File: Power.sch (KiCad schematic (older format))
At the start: 10 parts, among them U2 MCP1700T-3302E/TT_

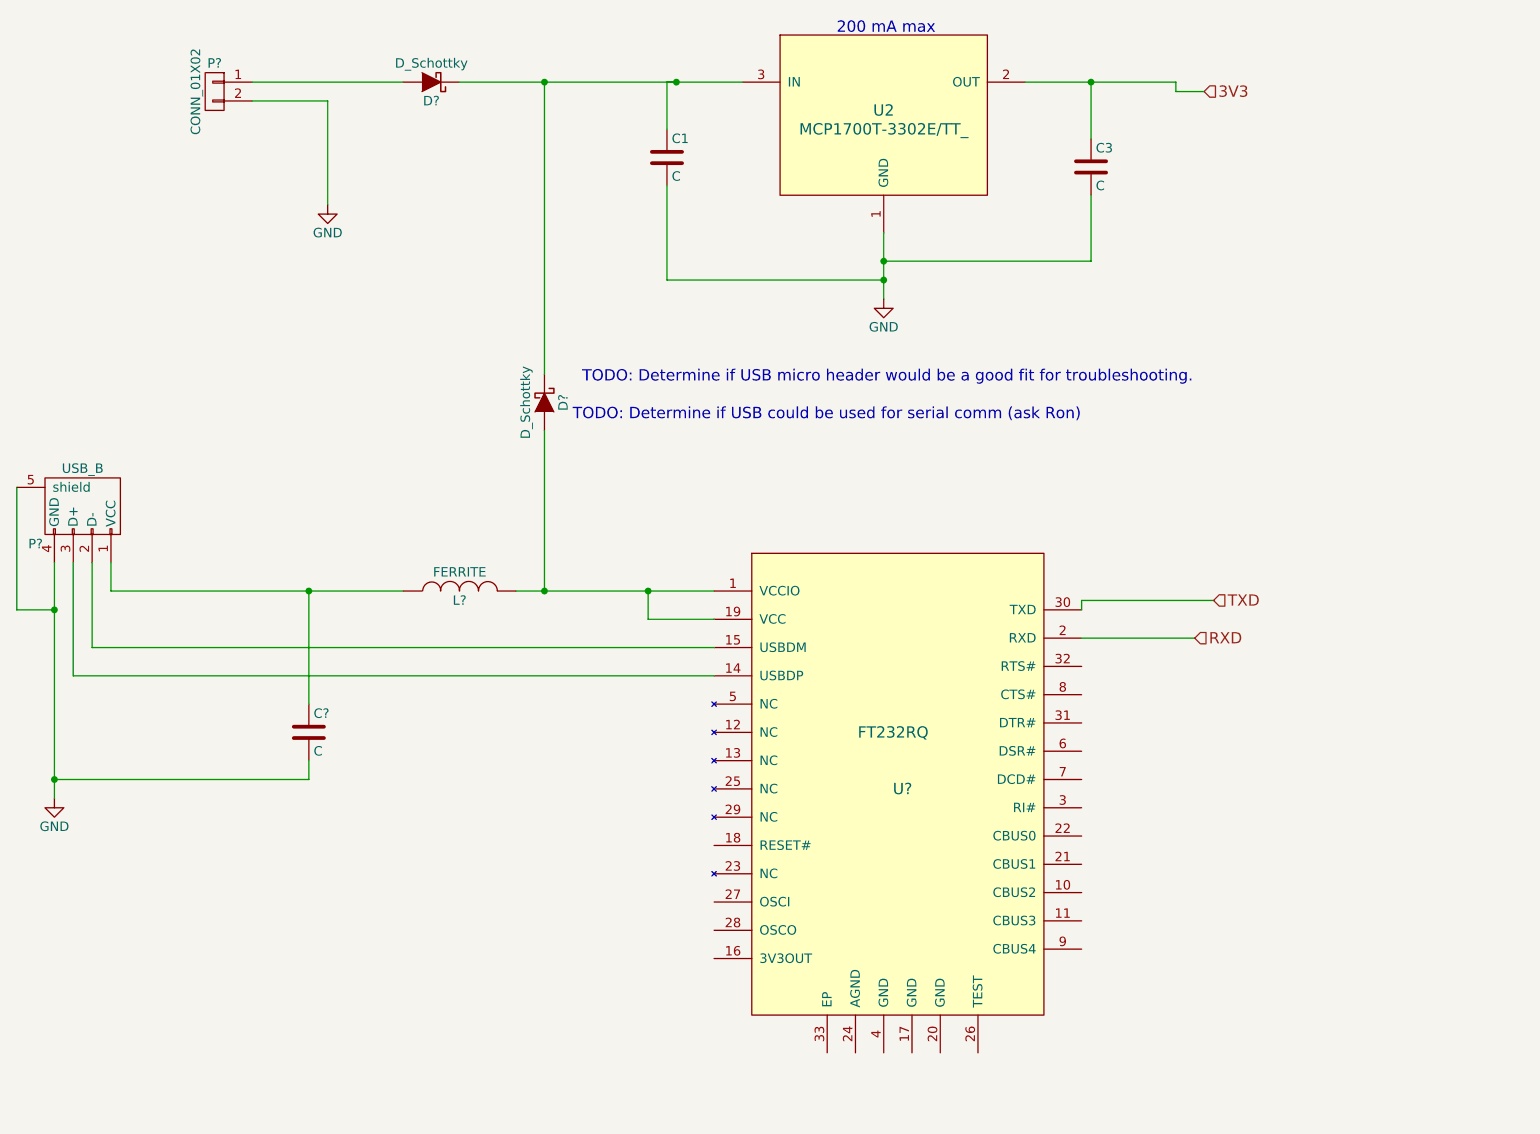
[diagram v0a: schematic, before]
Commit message: Added more decoupling caps, indicator LEDs and hooked reset into the FTDI chip
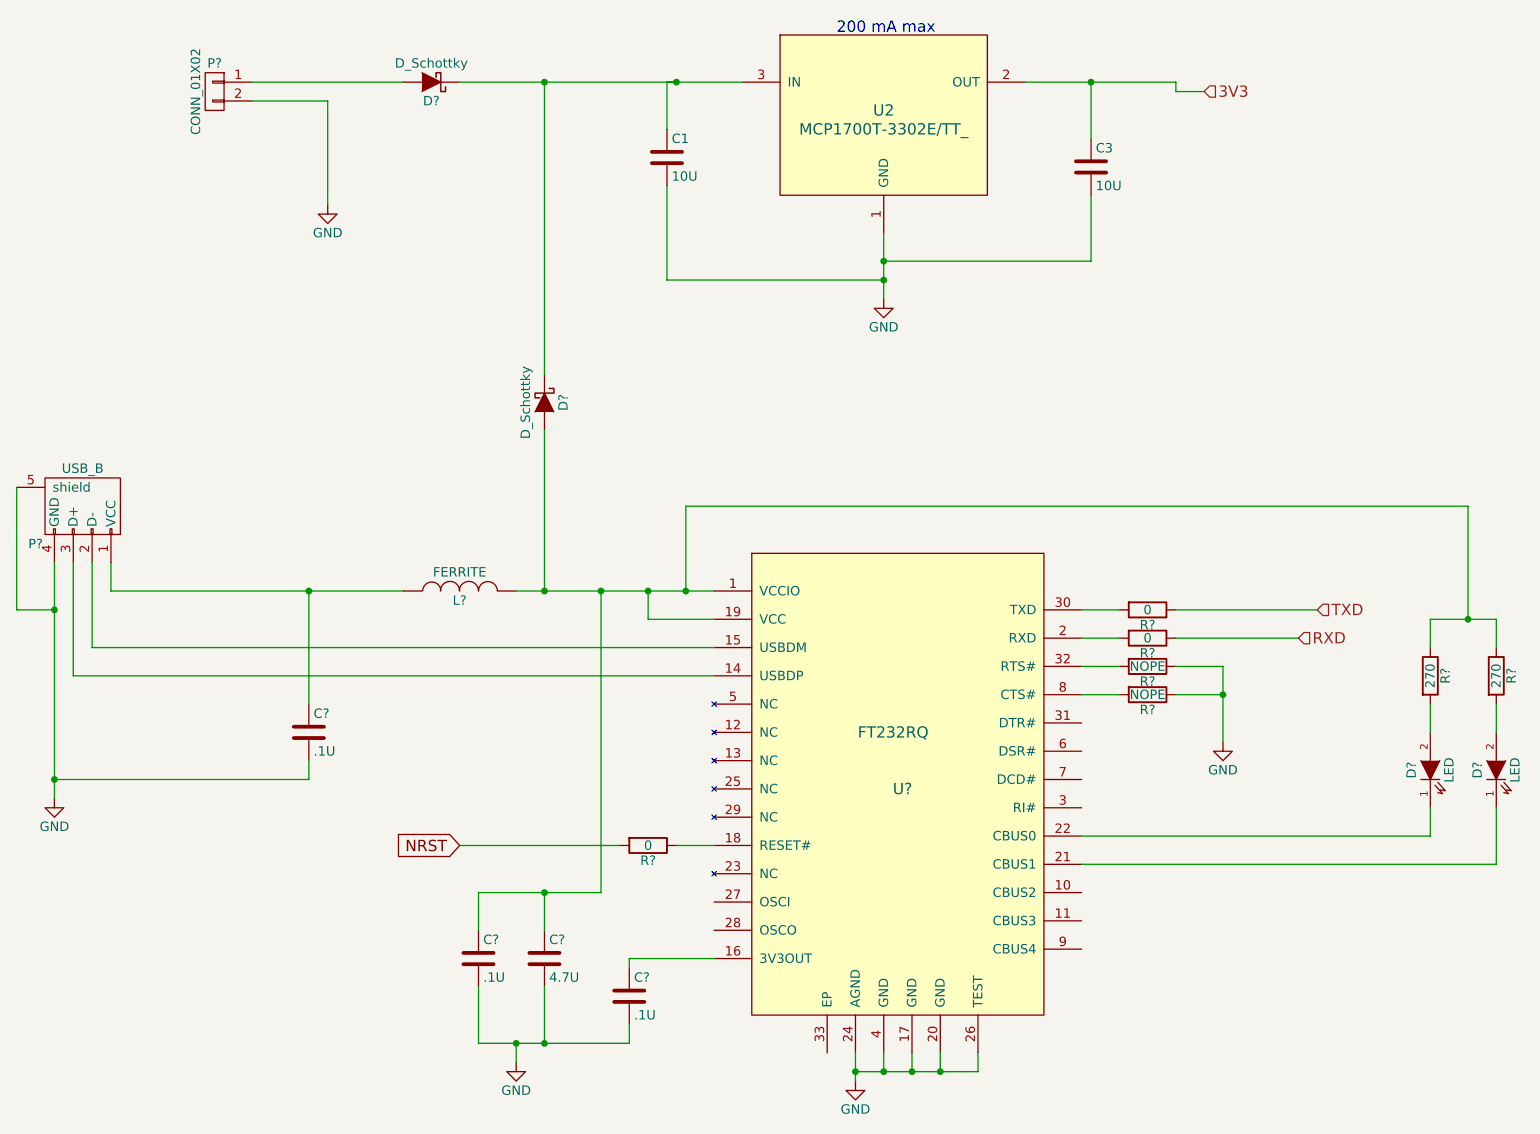
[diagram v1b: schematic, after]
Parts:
- added C?: 4.7U, symbol C
- added C? (x2): .1U, symbol C
- added D? (x2): LED, symbol LED
- added R? (x3): 0, symbol R
- added R? (x2): 270, symbol R
- added R? (x2): NOPE, symbol R
- C1, C3: value C -> 10U
- C?: value C -> .1U
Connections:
- net GND: now also U?.17 (GND), U?.20 (GND), U?.24 (AGND), U?.26 (TEST), U?.4 (GND), C?.2, C?.2, C?.2, R?.1, R?.1
- net RXD: now also R?.1; no longer U?.2 (RXD)
- net TXD: now also R?.1; no longer U?.30 (TXD)
- net at D?.2 (A), L?.2, U?.1 (VCCIO)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: now also C?.1, C?.1, R?.1, R?.1
- net at U?.16 (3V3OUT): now also C?.1
- net at U?.18 (RESET#): now also R?.1
- net at U?.21 (CBUS1): now also D?.1 (K)
- net at U?.22 (CBUS0): now also D?.1 (K)
- net at U?.32 (RTS#): now also R?.2
- net at U?.8 (CTS#): now also R?.2
- new net: R?.2, U?.2 (RXD)
- new net: R?.2, U?.30 (TXD)
- new net: D?.2 (A), R?.2 (x2)
- new net NRST: R?.2
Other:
- note removed: "TODO: Determine if USB could be used for serial comm (ask Ron)"
- note removed: "TODO: Determine if USB micro header would be a good fit for troubleshooting."

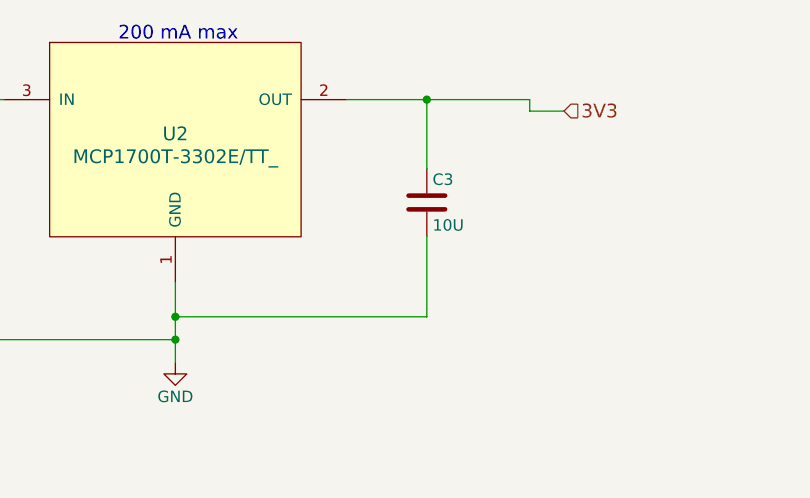
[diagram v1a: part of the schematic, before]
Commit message: Added headers and created a new sheet for communication headers
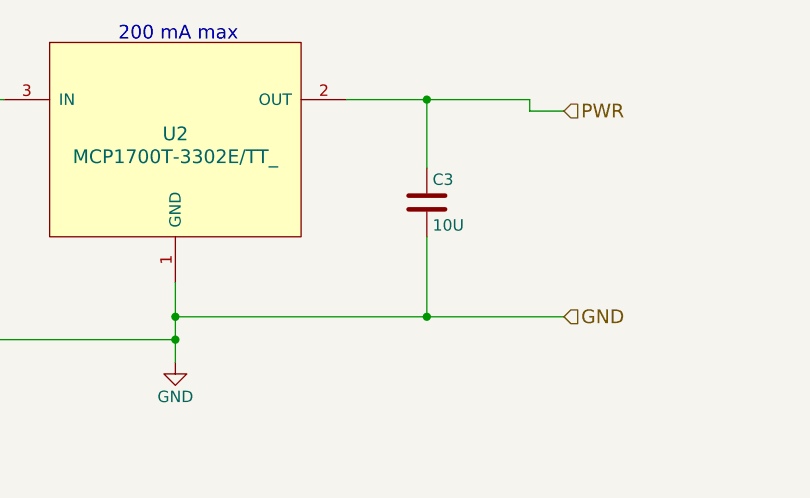
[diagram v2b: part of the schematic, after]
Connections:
- net 3V3 renamed PWR
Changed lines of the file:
@@
 $Descr A4 11693 8268
 encoding utf-8
-Sheet 2 2
+Sheet 2 3
 Title ""
 Date ""
@@
 	5500 1750 5500 2100
 Wire Wire Line
-	5500 1900 6600 1900
+	5500 1900 7200 1900
 Wire Wire Line
 	6600 1900 6600 1550
@@
 $EndComp
 Text HLabel 7200 1000 2    60   Input ~ 0
-3V3
+PWR
 $Comp
 L C C?
@@
 Wire Wire Line
 	7050 3750 7800 3750
+Connection ~ 6600 1900
+Text HLabel 7200 1900 2    60   Input ~ 0
+GND
 $EndSCHEMATC
